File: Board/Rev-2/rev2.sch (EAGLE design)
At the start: 56 parts, among them IC1 74HC595N, T1 2N3904, T2 2N3904, T3 2N3904, T4 2N3904, T5 2N3904, T6 2N3904, T7 2N3904, T8 2N3904

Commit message: Board Generated
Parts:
- removed SL1: Flash, con-amp-quick:MA02
- added FLASH, GND_SWITCH, VCC_SWITCH: TOGGLE_SWITCH, Toggle Switch:TOGGLE_SWITCH
- added PULLUP: 10kohm, resistor:R-EU_0204/7
- added SV1: (no value), con-lstb:MA04-1
- renumbered ESP-RESET to MCU-RESET, PHOTOREG to RESET_REG, R1 to PHOTO_REG, RESET to SETUP_MODE
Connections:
- new net N$55: GND_SWITCH.ON, SV1.1
- new net N$56: SV1.4, VCC_SWITCH.ON
- net 3.5V: now also FLASH.OFF, PULLUP.2
- net GND: now also FLASH.ON, GND_SWITCH.IN, PULLUP.1; no longer SL1.1
- net N$28: now also FLASH.IN; no longer SL1.2
- net RX: now also SV1.2
- net TX: now also SV1.3
- net VCC: now also VCC_SWITCH.IN

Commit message: board updated
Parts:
- SV1: device con-lstb:MA04-1 -> con-lstb:MA06-2
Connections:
- net 3.5V: now also SV1.4
- net CS0: now also SV1.6
- net GPIO10: now also SV1.7
- net GPIO5: now also SV1.5
- net GPIO9: now also SV1.9
- net MISO: now also SV1.8
- net MOSI: now also SV1.10
- net N$55: now also SV1.12; no longer SV1.1
- net N$56: now also SV1.2; no longer SV1.4
- net RX: now also SV1.3; no longer SV1.2
- net SCLK: now also SV1.11
- net TX: now also SV1.1; no longer SV1.3

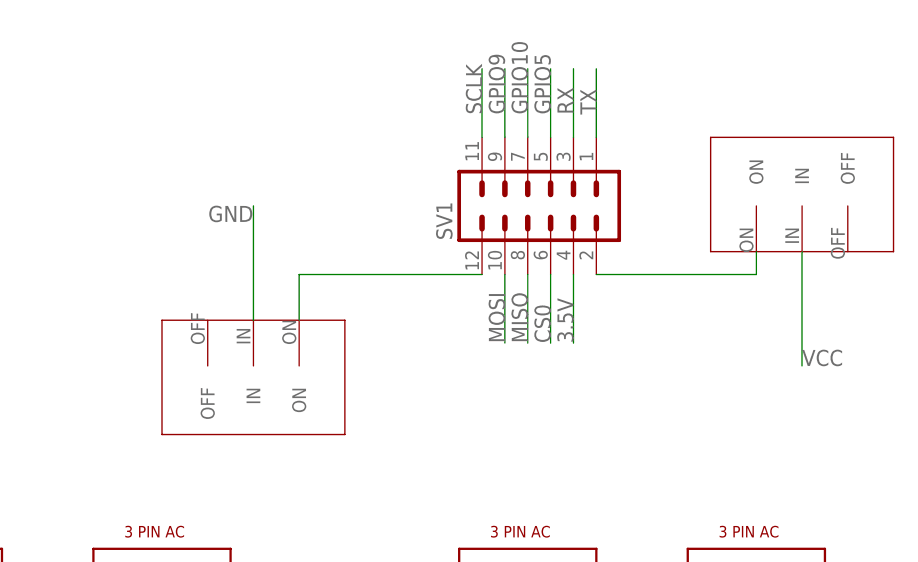
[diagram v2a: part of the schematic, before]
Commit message: Reconnect option added
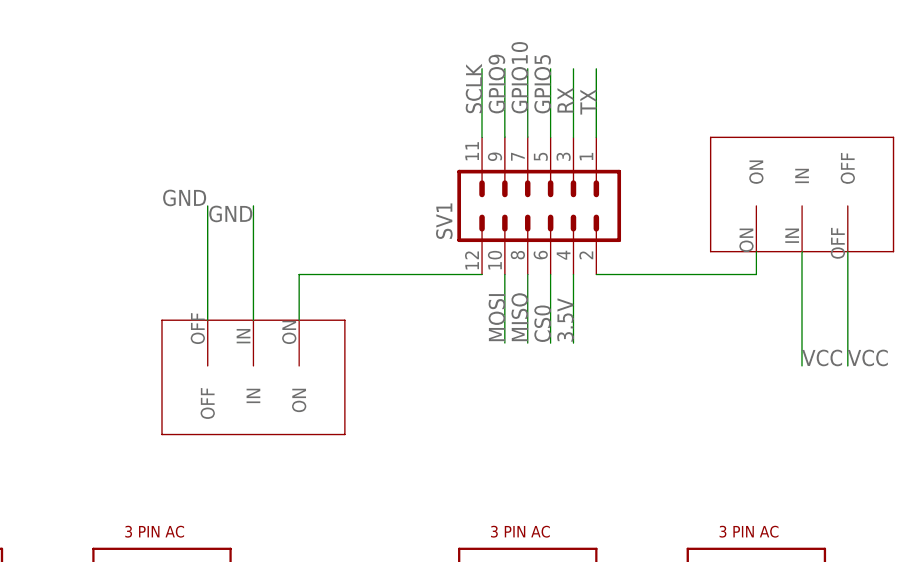
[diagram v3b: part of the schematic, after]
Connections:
- net GND: now also GND_SWITCH.OFF
- net VCC: now also VCC_SWITCH.OFF
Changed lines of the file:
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@@
 <?xml version="1.0" encoding="utf-8"?>
 <!DOCTYPE eagle SYSTEM "eagle.dtd">
-<eagle version="9.6.2">
+<eagle version="9.3.0">
 <drawing>
 <settings>
@@
 <grid distance="0.1" unitdist="inch" unit="inch" style="lines" multiple="1" display="no" altdistance="0.01" altunitdist="inch" altunit="inch"/>
 <layers>
-<layer number="1" name="Top" color="4" fill="1" visible="yes" active="no"/>
-<layer number="2" name="Route2" color="16" fill="1" visible="yes" active="no"/>
-<layer number="3" name="Route3" color="17" fill="1" visible="yes" active="no"/>
-<layer number="4" name="Route4" color="18" fill="1" visible="yes" active="no"/>
-<layer number="5" name="Route5" color="19" fill="1" visible="yes" active="no"/>
-<layer number="6" name="Route6" color="25" fill="1" visible="yes" active="no"/>
-<layer number="7" name="Route7" color="26" fill="1" visible="yes" active="no"/>
-<layer number="8" name="Route8" color="27" fill="1" visible="yes" active="no"/>
-<layer number="9" name="Route9" color="28" fill="1" visible="yes" active="no"/>
-<layer number="10" name="Route10" color="29" fill="1" visible="yes" active="no"/>
-<layer number="11" name="Route11" color="30" fill="1" visible="yes" active="no"/>
-<layer number="12" name="Route12" color="20" fill="1" visible="yes" active="no"/>
-<layer number="13" name="Route13" color="21" fill="1" visible="yes" active="no"/>
-<layer number="14" name="Route14" color="22" fill="1" visible="yes" active="no"/>
-<layer number="15" name="Route15" color="23" fill="1" visible="yes" active="no"/>
-<layer number="16" name="Bottom" color="1" fill="1" visible="yes" active="no"/>
-<layer number="17" name="Pads" color="2" fill="1" visible="yes" active="no"/>
-<layer number="18" name="Vias" color="2" fill="1" visible="yes" active="no"/>
-<layer number="19" name="Unrouted" color="6" fill="1" visible="yes" active="no"/>
-<layer number="20" name="Dimension" color="24" fill="1" visible="yes" active="no"/>
-<layer number="21" name="tPlace" color="7" fill="1" visible="yes" active="no"/>
-<layer number="22" name="bPlace" color="7" fill="1" visible="yes" active="no"/>
-<layer number="23" name="tOrigins" color="15" fill="1" visible="yes" active="no"/>
-<layer number="24" name="bOrigins" color="15" fill="1" visible="yes" active="no"/>
-<layer number="25" name="tNames" color="7" fill="1" visible="yes" active="no"/>
-<layer number="26" name="bNames" color="7" fill="1" visible="yes" active="no"/>
-<layer number="27" name="tValues" color="7" fill="1" visible="yes" active="no"/>
-<layer number="28" name="bValues" color="7" fill="1" visible="yes" active="no"/>
+<layer number="1" name="Top" color="4" fill="1" visible="no" active="no"/>
+<layer number="2" name="Route2" color="16" fill="1" visible="no" active="no"/>
+<layer number="3" name="Route3" color="17" fill="1" visible="no" active="no"/>
+<layer number="4" name="Route4" color="18" fill="1" visible="no" active="no"/>
+<layer number="5" name="Route5" color="19" fill="1" visible="no" active="no"/>
+<layer number="6" name="Route6" color="25" fill="1" visible="no" active="no"/>
+<layer number="7" name="Route7" color="26" fill="1" visible="no" active="no"/>
+<layer number="8" name="Route8" color="27" fill="1" visible="no" active="no"/>
+<layer number="9" name="Route9" color="28" fill="1" visible="no" active="no"/>
+<layer number="10" name="Route10" color="29" fill="1" visible="no" active="no"/>
+<layer number="11" name="Route11" color="30" fill="1" visible="no" active="no"/>
+<layer number="12" name="Route12" color="20" fill="1" visible="no" active="no"/>
+<layer number="13" name="Route13" color="21" fill="1" visible="no" active="no"/>
+<layer number="14" name="Route14" color="22" fill="1" visible="no" active="no"/>
+<layer number="15" name="Route15" color="23" fill="1" visible="no" active="no"/>
+<layer number="16" name="Bottom" color="1" fill="1" visible="no" active="no"/>
+<layer number="17" name="Pads" color="2" fill="1" visible="no" active="no"/>
+<layer number="18" name="Vias" color="2" fill="1" visible="no" active="no"/>
+<layer number="19" name="Unrouted" color="6" fill="1" visible="no" active="no"/>
+<layer number="20" name="Dimension" color="24" fill="1" visible="no" active="no"/>
+<layer number="21" name="tPlace" color="7" fill="1" visible="no" active="no"/>
+<layer number="22" name="bPlace" color="7" fill="1" visible="no" active="no"/>
+<layer number="23" name="tOrigins" color="15" fill="1" visible="no" active="no"/>
+<layer number="24" name="bOrigins" color="15" fill="1" visible="no" active="no"/>
+<layer number="25" name="tNames" color="7" fill="1" visible="no" active="no"/>
+<layer number="26" name="bNames" color="7" fill="1" visible="no" active="no"/>
+<layer number="27" name="tValues" color="7" fill="1" visible="no" active="no"/>
+<layer number="28" name="bValues" color="7" fill="1" visible="no" active="no"/>
 <layer number="29" name="tStop" color="7" fill="3" visible="no" active="no"/>
 <layer number="30" name="bStop" color="7" fill="6" visible="no" active="no"/>
@@
 <layer number="35" name="tGlue" color="7" fill="4" visible="no" active="no"/>
 <layer number="36" name="bGlue" color="7" fill="5" visible="no" active="no"/>
-<layer number="37" name="tTest" color="7" fill="1" visible="yes" active="no"/>
-<layer number="38" name="bTest" color="7" fill="1" visible="yes" active="no"/>
+<layer number="37" name="tTest" color="7" fill="1" visible="no" active="no"/>
+<layer number="38" name="bTest" color="7" fill="1" visible="no" active="no"/>
 <layer number="39" name="tKeepout" color="4" fill="11" visible="no" active="no"/>
 <layer number="40" name="bKeepout" color="1" fill="11" visible="no" active="no"/>
@@
 <layer number="44" name="Drills" color="7" fill="1" visible="no" active="no"/>
 <layer number="45" name="Holes" color="7" fill="1" visible="no" active="no"/>
-<layer number="46" name="Milling" color="3" fill="1" visible="yes" active="no"/>
-<layer number="47" name="Measures" color="7" fill="1" visible="yes" active="no"/>
-<layer number="48" name="Document" color="7" fill="1" visible="yes" active="no"/>
-<layer number="49" name="Reference" color="7" fill="1" visible="yes" active="no"/>
-<layer number="50" name="dxf" color="7" fill="1" visible="yes" active="no"/>
-<layer number="51" name="tDocu" color="7" fill="1" visible="yes" active="no"/>
-<layer number="52" name="bDocu" color="7" fill="1" visible="yes" active="no"/>
-<layer number="53" name="tGND_GNDA" color="7" fill="9" visible="yes" active="no"/>
-<layer number="54" name="bGND_GNDA" color="1" fill="9" visible="yes" active="no"/>
-<layer number="56" name="wert" color="7" fill="1" visible="yes" active="no"/>
-<layer number="57" name="tCAD" color="7" fill="1" visible="yes" active="no"/>
-<layer number="59" name="tCarbon" color="7" fill="1" visible="yes" active="no"/>
-<layer number="60" name="bCarbon" color="7" fill="1" visible="yes" active="no"/>
+<layer number="46" name="Milling" color="3" fill="1" visible="no" active="no"/>
+<layer number="47" name="Measures" color="7" fill="1" visible="no" active="no"/>
+<layer number="48" name="Document" color="7" fill="1" visible="no" active="no"/>
+<layer number="49" name="Reference" color="7" fill="1" visible="no" active="no"/>
+<layer number="50" name="dxf" color="7" fill="1" visible="no" active="no"/>
+<layer number="51" name="tDocu" color="7" fill="1" visible="no" active="no"/>
+<layer number="52" name="bDocu" color="7" fill="1" visible="no" active="no"/>
+<layer number="53" name="tGND_GNDA" color="7" fill="9" visible="no" active="no"/>
+<layer number="54" name="bGND_GNDA" color="1" fill="9" visible="no" active="no"/>
+<layer number="56" name="wert" color="7" fill="1" visible="no" active="no"/>
+<layer number="57" name="tCAD" color="7" fill="1" visible="no" active="no"/>
+<layer number="59" name="tCarbon" color="7" fill="1" visible="no" active="no"/>
+<layer number="60" name="bCarbon" color="7" fill="1" visible="no" active="no"/>
 <layer number="88" name="SimResults" color="9" fill="1" visible="yes" active="yes"/>
 <layer number="89" name="SimProbes" color="9" fill="1" visible="yes" active="yes"/>
@@
 <label x="45.72" y="68.58" size="1.778" layer="95"/>
 </segment>
+<segment>
+<pinref part="GND_SWITCH" gate="G$1" pin="OFF"/>
+<wire x1="134.62" y1="127" x2="134.62" y2="139.7" width="0.1524" layer="91"/>
+<label x="129.54" y="139.7" size="1.778" layer="95"/>
+</segment>
 </net>
 <net name="N$1" class="0">
@@
 <label x="200.66" y="121.92" size="1.778" layer="95"/>
 </segment>
-</net>
+<segment>
+<pinref part="VCC_SWITCH" gate="G$1" pin="OFF"/>
+<wire x1="205.74" y1="134.62" x2="205.74" y2="121.92" width="0.1524" layer="91"/>
+<label x="205.74" y="121.92" size="1.778" layer="95"/>
+</segment>
+</net>

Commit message: Board file updated
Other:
- note added: "Peripheral"
- note added: "Power Supply"
- note added: "Processer"
- note added: "Relay"
- note added: "Sensor"
- note added: "Shift Register"
- moved on the sheet: C1, D1, D2, D3, D4, D5, D6, D7, D8, ESP8266, HLK-5M05, IC1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
